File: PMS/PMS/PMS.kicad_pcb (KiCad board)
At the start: 4 copper layers, 97.5 x 67.5 mm, 35 parts, among them IC1 TMCS1107A1BQDRQ1, J1 XT90PW-M, J2 OSTYK44105030, J4 XT60PW-F, J5 XT90PW-F, J6 Conn_01x03_Male, J7 Conn_01x02_Male, U1 ADC101C027CIMK, U2 ADC101C027CIMK, U4 REF195

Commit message: More changes to grounding
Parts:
- moved C9 0.10 mm to (107.8, 91.5)
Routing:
- net GND: track 24.1 -> 24.2 mm, vias 50 -> 51
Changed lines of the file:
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@@
   (net 19 "unconnected-(U4-Pad8)")
   (footprint "Capacitor_SMD:C_0805_2012Metric_Pad1.18x1.45mm_HandSolder" (layer "F.Cu")
-    (at 107.9 91.5)
+    (at 107.8 91.5)
     (descr "Capacitor SMD 0805 (2012 Metric), square (rectangular) end terminal, IPC_7351 nominal with elongated pad for handsoldering. (Body size source: IPC-SM-782 page 76, https://www.pcb-3d.com/wordpress/wp-content/uploads/ipc-sm-782a_amendment_1_and_2.pdf, https://docs.google.com/spreadsheets/d/1BsfQQcO9C6DZCsRaXUlFlo91Tg2WpOkGARC1WS5S8t0/edit?usp=sharing), generated with kicad-footprint-generator")
     (tags "capacitor handsolder")
@@
   (segment (start 104.9375 92.85) (end 106.3 92.85) (width 0.5) (layer "F.Cu") (net 2))
   (segment (start 97.7625 93.9875) (end 97.75 94) (width 0.5) (layer "F.Cu") (net 2))
+  (segment (start 108.8375 92.5375) (end 108.8375 91.5) (width 1) (layer "F.Cu") (net 2))
   (segment (start 106.3 92.85) (end 106.35 92.9) (width 0.5) (layer "F.Cu") (net 2))
   (segment (start 102.35 72.5625) (end 102.3625 72.55) (width 1) (layer "F.Cu") (net 2))
@@
   (segment (start 98.95 93.9875) (end 97.7625 93.9875) (width 0.5) (layer "F.Cu") (net 2))
   (segment (start 95.1125 90.3625) (end 95.1125 91.75) (width 1) (layer "F.Cu") (net 2))
-  (segment (start 110 91.5) (end 108.9375 91.5) (width 1) (layer "F.Cu") (net 2))
   (segment (start 104.095 76.211) (end 104.095 77.695) (width 0.5) (layer "F.Cu") (net 2))
   (segment (start 98.6625 88.5125) (end 98.65 88.5) (width 1) (layer "F.Cu") (net 2))
   (segment (start 90.1625 71.4) (end 89.1 71.4) (width 1) (layer "F.Cu") (net 2))
+  (segment (start 108.95 92.65) (end 108.8375 92.5375) (width 1) (layer "F.Cu") (net 2))
   (segment (start 108.2 95.6) (end 107.0875 95.6) (width 1) (layer "F.Cu") (net 2))
   (via (at 97.85 106.7) (size 0.8) (drill 0.4) (layers "F.Cu" "B.Cu") (free) (net 2))
@@
   (via (at 98.55 107.15) (size 0.8) (drill 0.4) (layers "F.Cu" "B.Cu") (free) (net 2))
   (via (at 97.75 94) (size 0.8) (drill 0.4) (layers "F.Cu" "B.Cu") (free) (net 2))
+  (via (at 110.05 91.25) (size 0.8) (drill 0.4) (layers "F.Cu" "B.Cu") (free) (net 2))
   (via (at 103.6 94.95) (size 0.8) (drill 0.4) (layers "F.Cu" "B.Cu") (free) (net 2))
   (via (at 101.9 94.95) (size 0.8) (drill 0.4) (layers "F.Cu" "B.Cu") (free) (net 2))
@@
   (via (at 89.1 71.4) (size 0.8) (drill 0.4) (layers "F.Cu" "B.Cu") (net 2))
   (via (at 98.65 88.5) (size 0.8) (drill 0.4) (layers "F.Cu" "B.Cu") (net 2))
-  (via (at 110 91.5) (size 0.8) (drill 0.4) (layers "F.Cu" "B.Cu") (net 2))
+  (via (at 108.95 92.65) (size 0.8) (drill 0.4) (layers "F.Cu" "B.Cu") (net 2))
   (via (at 99.7 84.6) (size 0.8) (drill 0.4) (layers "F.Cu" "B.Cu") (net 2))
   (via (at 102.3 99.1) (size 0.8) (drill 0.4) (layers "F.Cu" "B.Cu") (free) (net 2))
@@
   (via (at 102.95 68) (size 0.8) (drill 0.4) (layers "F.Cu" "B.Cu") (free) (net 7))
   (via (at 105.2 65.75) (size 0.8) (drill 0.4) (layers "F.Cu" "B.Cu") (free) (net 7))
-  (segment (start 104.9375 91.9) (end 106.4625 91.9) (width 0.5) (layer "F.Cu") (net 9))
+  (segment (start 104.9375 91.9) (end 106.3625 91.9) (width 0.5) (layer "F.Cu") (net 9))
+  (segment (start 106.3625 91.9) (end 106.7625 91.5) (width 0.5) (layer "F.Cu") (net 9))
   (segment (start 106.635 91.2725) (end 106.635 76.211) (width 0.5) (layer "F.Cu") (net 9))
-  (segment (start 106.4625 91.9) (end 106.8625 91.5) (width 0.5) (layer "F.Cu") (net 9))
   (segment (start 101.0375 93.8) (end 100.85 93.9875) (width 0.25) (layer "F.Cu") (net 10))
   (segment (start 101.6 102) (end 101.3 101.7) (width 1) (layer "F.Cu") (net 10))
@@
   )
   (zone (net 2) (net_name "GND") (layer "In1.Cu") (hatch edge 0.508)
-    (connect_pads (clearance 0.508))
-    (min_thickness 0.254) (filled_areas_thickness no)
-    (fill yes (thermal_gap 0.508) (thermal_bridge_width 0.508))
-    (polygon
-      (pts
-        (xy 110.5 108.25)
-        (xy 88.85 108.25)
-        (xy 88.85 74.55)
-        (xy 110.5 74.55)
-      )
-    )
-  )
-  (zone (net 2) (net_name "GND") (layer "In1.Cu") (hatch edge 0.508)
     (priority 1)
     (connect_pads (clearance 0.508))
@@
         (xy 108.75 74)
         (xy 108.75 74.55)
+        (xy 110.5 74.55)
+        (xy 110.5 88.55)
+        (xy 107 88.55)
+        (xy 107 90.8)
+        (xy 110.5 90.8)
+        (xy 110.5 108.25)
+        (xy 88.85 108.25)
+        (xy 88.85 90.8)
+        (xy 92.35 90.8)
+        (xy 92.35 88.55)
+        (xy 88.85 88.55)
+        (xy 88.85 74.55)
         (xy 91.2 74.55)
         (xy 91.2 74)

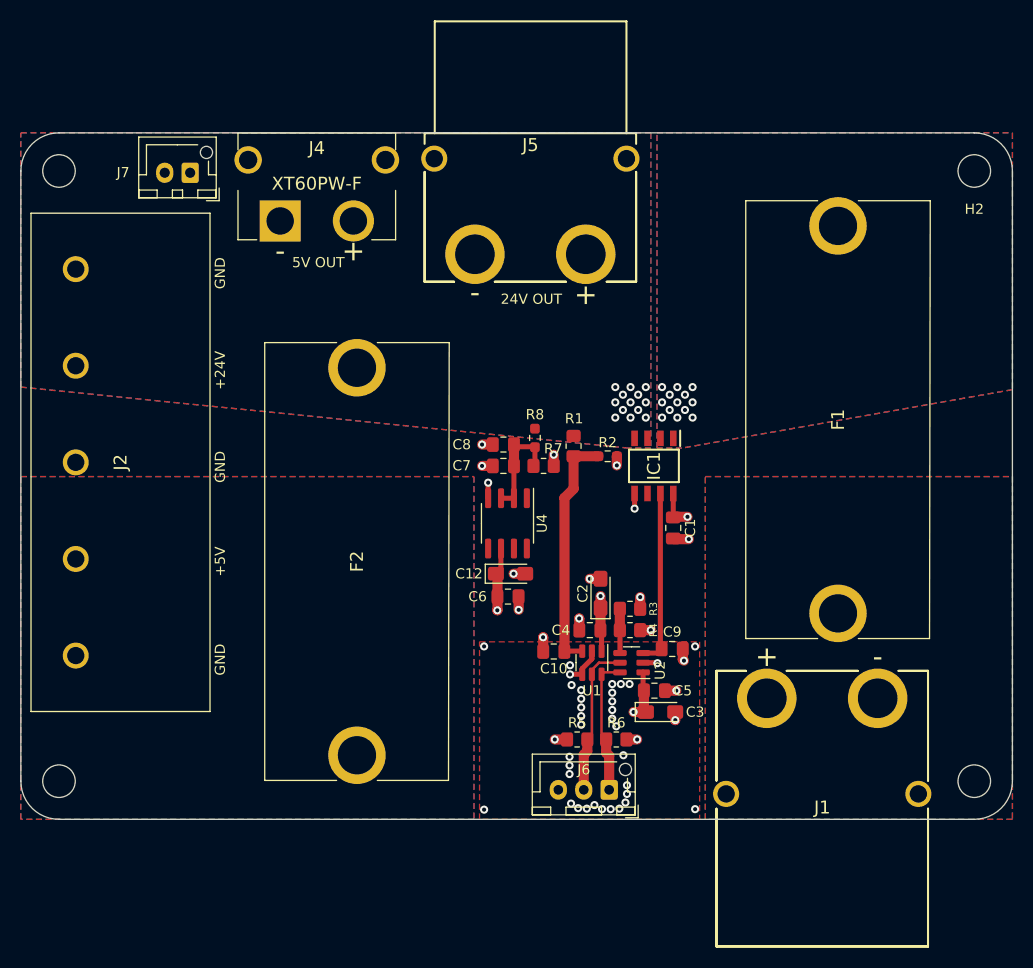
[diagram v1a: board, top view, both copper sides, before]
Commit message: increased distance between planes. Improved top GND plane for analog portion of board. simplified some geometries. VIAS.
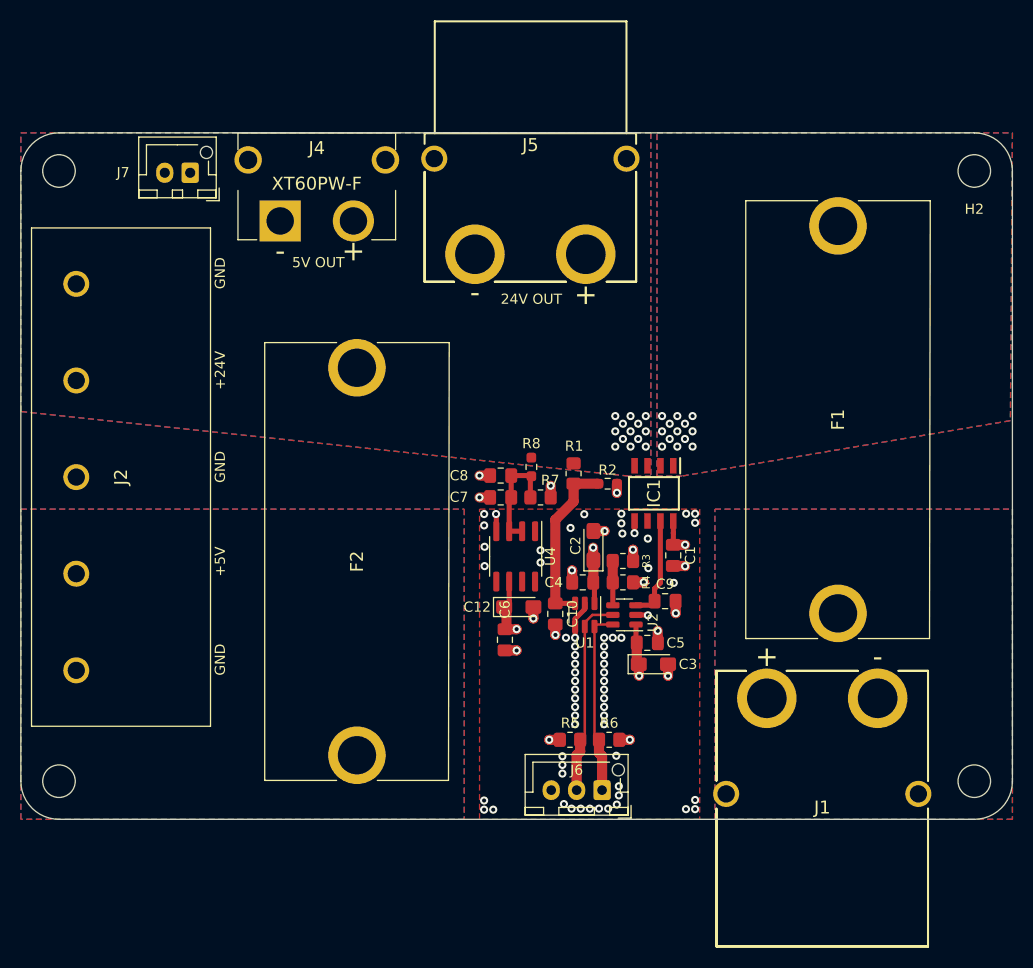
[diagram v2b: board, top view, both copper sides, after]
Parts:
- moved C3 4.75 mm to (106.0, 93.0)
- moved C4 4.75 mm to (99.0, 85.0)
- moved C9 4.75 mm to (107.1, 86.8)
- moved R3 4.75 mm to (103.0, 82.8)
- moved R4 4.75 mm to (103.0, 85.0)
- moved C2 4.75 mm to (100.0, 81.3)
- moved C5 4.75 mm to (105.3, 90.9)
- moved U1 4.75 mm to (99.2, 88.2)
- moved U2 4.75 mm to (103.1, 88.2)
- moved C6 4.26 mm to (91.3, 90.6), turned to -90 degrees
- moved C10 3.70 mm to (96.3, 88.0), turned to -90 degrees
- moved C12 3.37 mm to (92.7, 87.4)
- moved U4 3.35 mm to (92.4, 82.4)
- moved R7 3.11 mm to (94.8, 76.6)
- moved C7 3.11 mm to (90.9, 76.6)
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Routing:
- net Net-(C9-Pad1): track 17.1 -> 10.1 mm
- net Net-(C10-Pad1): track 23.7 -> 16.9 mm
- net SCL: track 14.1 -> 19.2 mm
- net SDA: track 12.9 -> 17.7 mm
- net Net-(C7-Pad2): track 9.73 -> 11.0 mm
- net GND: track 24.2 -> 23.5 mm, vias 51 -> 78

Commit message: HOLY MOLY! Adding many, many vias for thermals and for EMI. Fencing spacing was altered to max wavelength / 40.
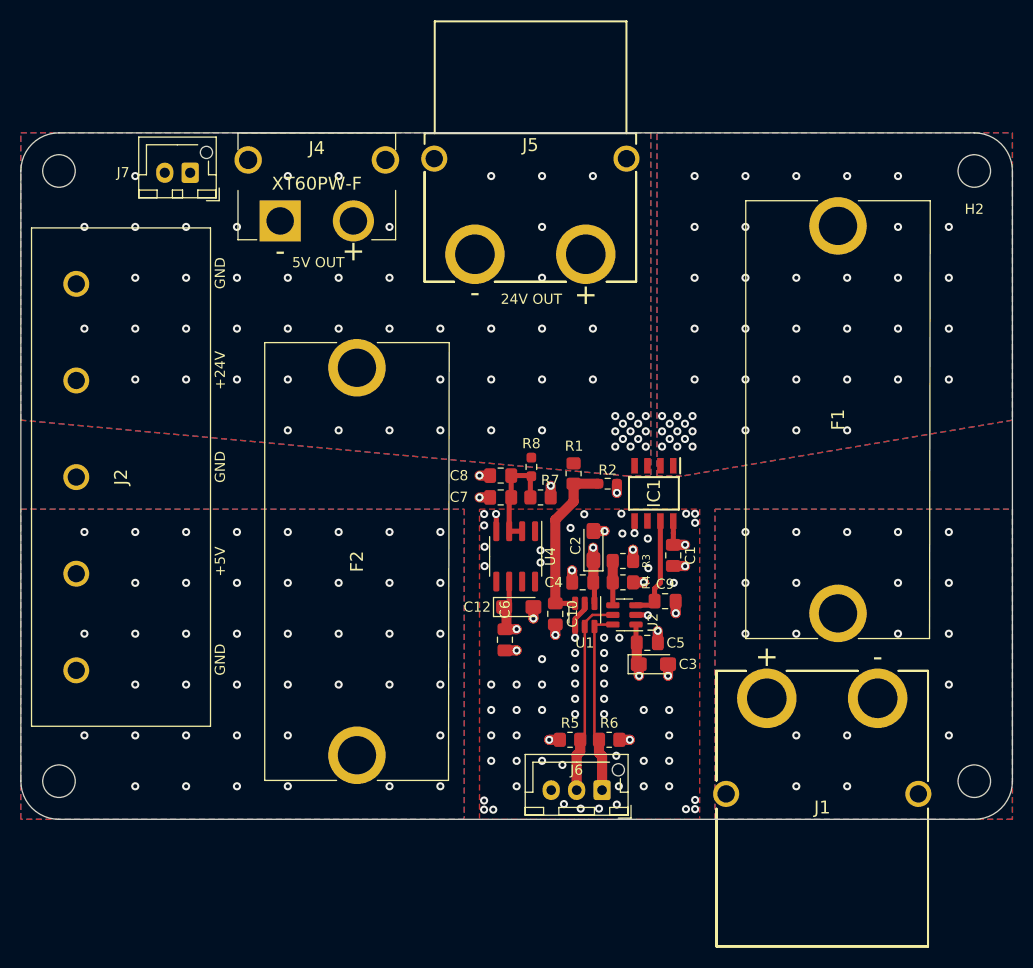
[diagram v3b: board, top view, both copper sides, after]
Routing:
- net GND: vias 78 -> 79
- net 24V_OUT: vias 13 -> 57
- net +BATT: vias 0 -> 19
- net +5VP: vias 0 -> 42
- net +24V: vias 13 -> 43

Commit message: cleanup
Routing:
- net Net-(C7-Pad2): track 11.0 -> 10.4 mm
- net GND: track 23.5 -> 23.4 mm, vias 79 -> 72
